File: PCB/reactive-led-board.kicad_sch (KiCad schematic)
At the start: 8 parts, among them J1 Conn_01x03_Socket, U1 XIAO-ESP32-S3-DIP, U2 SN74AHCT125N

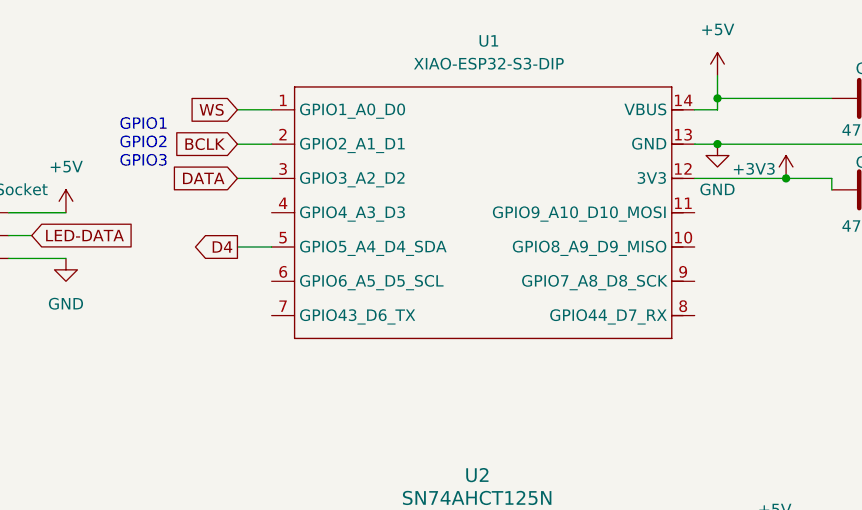
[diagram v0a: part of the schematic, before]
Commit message: routed the treaces and selected the parts i am going to use.
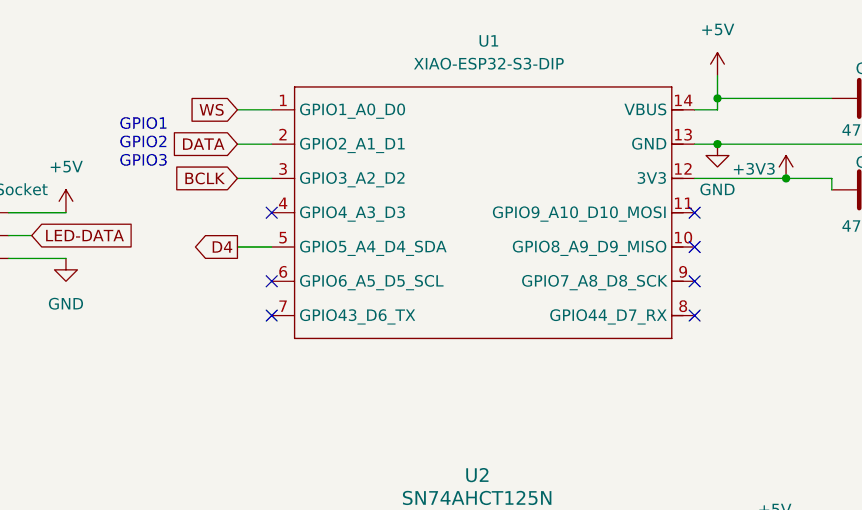
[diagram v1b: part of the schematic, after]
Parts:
- C1: footprint (none) -> Capacitor_THT:C_Rect_L7.2mm_W2.5mm_P5.00mm
- C2, C3: footprint (none) -> Capacitor_THT:CP_Radial_D8.0mm_P3.50mm
- R1: footprint (none) -> Resistor_THT:R_Axial_DIN0204_L3.6mm_D1.6mm_P1.90mm_Vertical
- U1: footprint Seeed_Studio_XIAO_Series:XIAO-ESP32-S3-DIP -> Seeed Studio XIAO Series Library:XIAO-ESP32-S3-DIP
- U2: footprint N14 -> sn74ahct125n:N14
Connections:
- net BCLK: now also U1.3 (GPIO3_A2_D2); no longer U1.2 (GPIO2_A1_D1)
- net DATA: now also U1.2 (GPIO2_A1_D1); no longer U1.3 (GPIO3_A2_D2)
- no-connect marks 3 -> 10

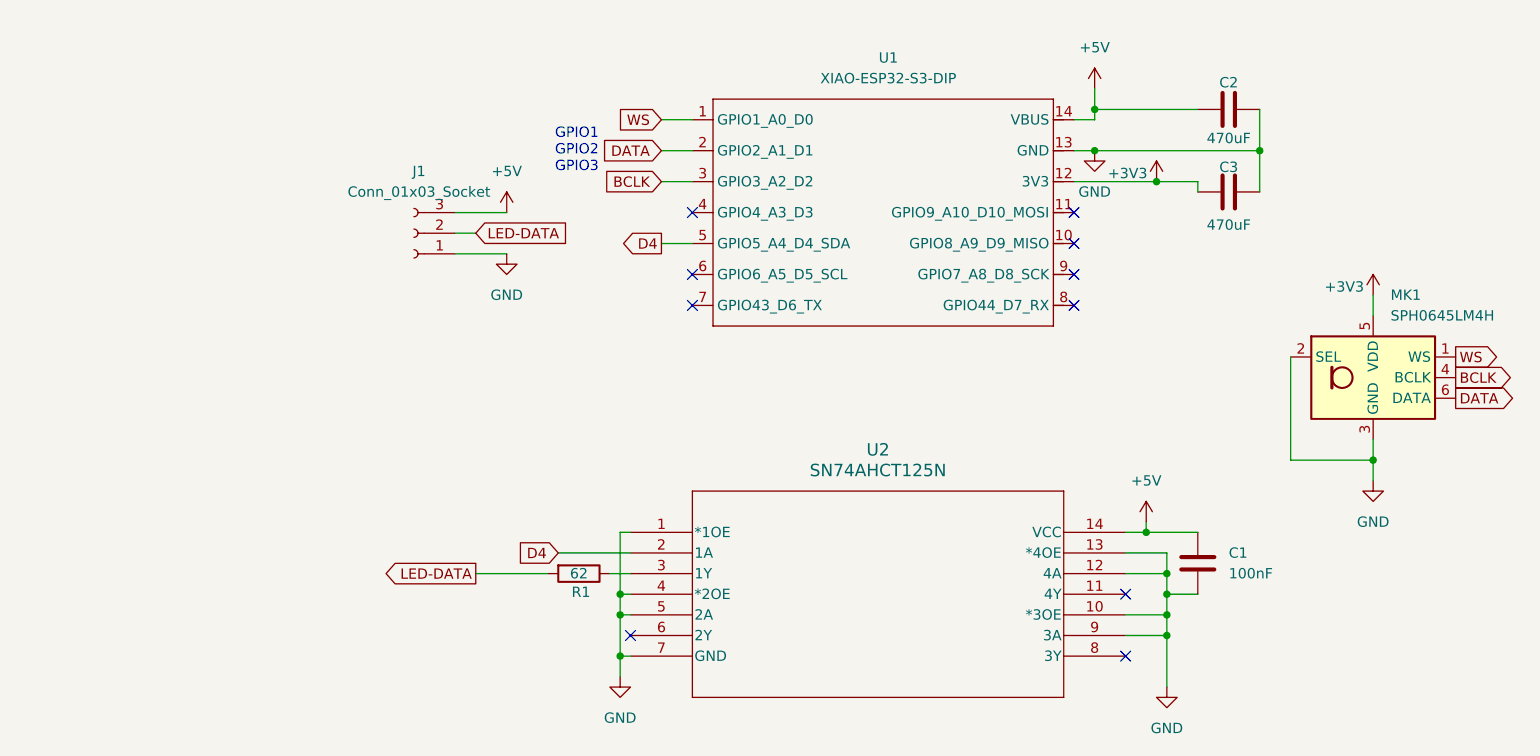
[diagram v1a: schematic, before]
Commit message: added 3d model for the xiao and added the connector for the mic module
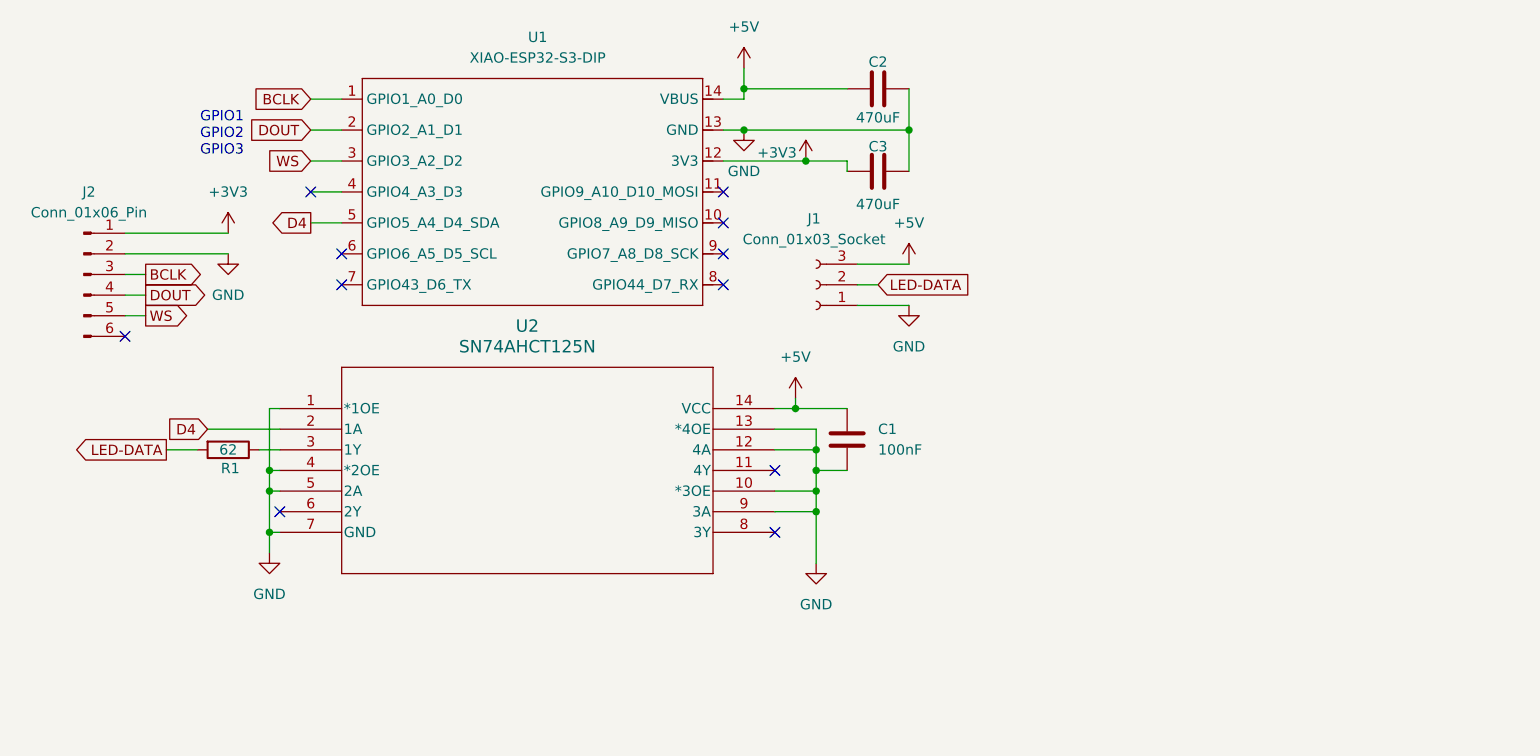
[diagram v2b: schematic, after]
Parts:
- removed MK1: SPH0645LM4H, Sensor_Audio:Knowles_SPH0645LM4H-6_3.5x2.65mm, symbol Sensor_Audio:SPH0645LM4H
- added J2: Conn_01x06_Pin, Connector_PinHeader_2.54mm:PinHeader_1x06_P2.54mm_Vertical, symbol Connector:Conn_01x06_Pin
- J1: footprint Connector_PinHeader_1.00mm:PinHeader_1x03_P1.00mm_Vertical -> Connector_PinHeader_2.54mm:PinHeader_1x03_P2.54mm_Vertical
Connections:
- net +3V3: now also J2.1 (Pin_1)
- net BCLK: now also U1.1 (GPIO1_A0_D0), J2.3 (Pin_3); no longer U1.3 (GPIO3_A2_D2)
- net GND: now also J2.2 (Pin_2)
- net WS: now also U1.3 (GPIO3_A2_D2), J2.5 (Pin_5); no longer U1.1 (GPIO1_A0_D0)
- net DATA renamed DOUT
- net DOUT: now also J2.4 (Pin_4)
- no-connect marks 10 -> 11
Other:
- moved on the sheet: C1, C2, C3, J1, R1, U1, U2

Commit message: did some hard ware changes and update bom swaped to using a screw terminal and updated the links in the bom to match with the leds i am going to use
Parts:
- J1: footprint Connector_PinHeader_2.54mm:PinHeader_1x03_P2.54mm_Vertical -> custom_screw_terminals:691137710003
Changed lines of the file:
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@@
 			)
 		)
-		(property "Footprint" "Connector_PinHeader_2.54mm:PinHeader_1x03_P2.54mm_Vertical"
+		(property "Footprint" "custom_screw_terminals:691137710003"
 			(at 111.76 43.18 0)
 			(hide yes)
